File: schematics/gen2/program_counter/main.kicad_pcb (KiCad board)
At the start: 2 copper layers, 100 x 89.5 mm, 16 parts, among them U1 74HC00, U2 74HC193, U3 74HC193, U4 74HC193, U5 74HC193, U6 74HC245, U7 74HC245

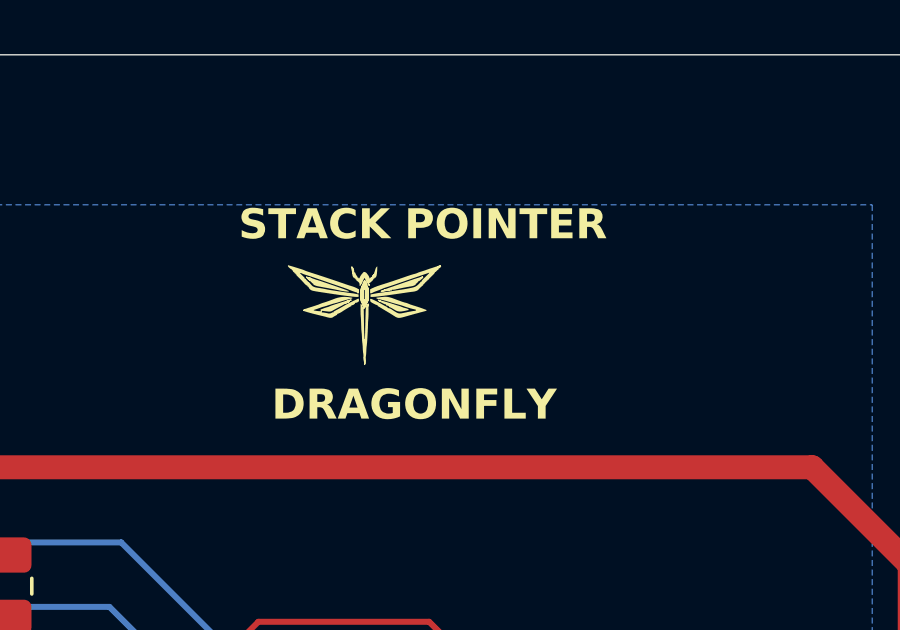
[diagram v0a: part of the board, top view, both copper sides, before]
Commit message: (feat) stack pointer and program counter pcb, QA needed.
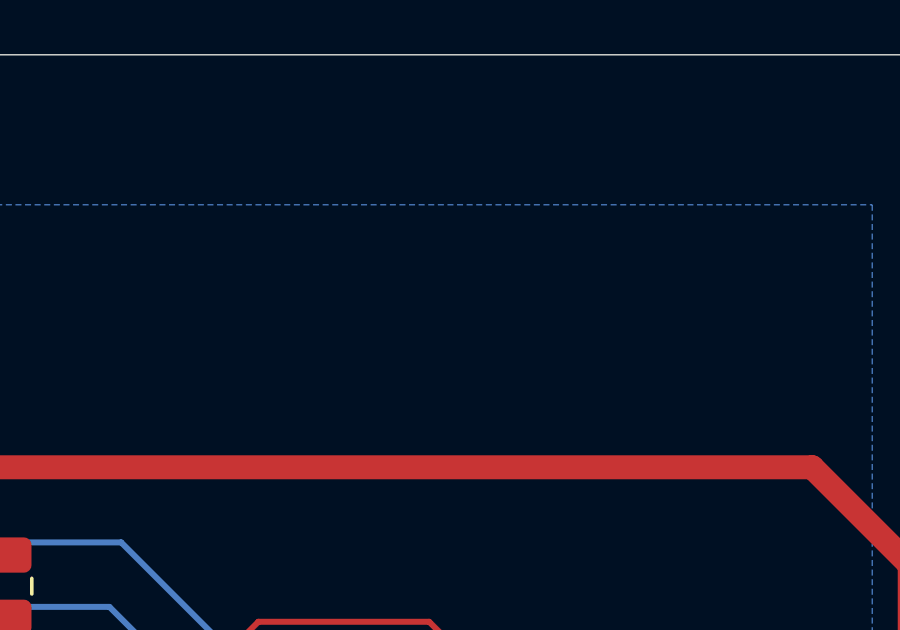
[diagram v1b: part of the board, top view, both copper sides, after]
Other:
- board text removed: "DRAGONFLY"
- board text removed: "STACK POINTER"
